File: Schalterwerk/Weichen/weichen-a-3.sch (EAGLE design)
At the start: 24 parts, among them Q1 P-MOSFET, Q2 P-MOSFET, X1 PHNX_4P_508CONN_1017493, X2 IO-HAT, X3 PHNX_4P_350CONN_1984989_PXC, X4 PHNX_4P_350CONN_1984989_PXC, X5 RJ45-JACK

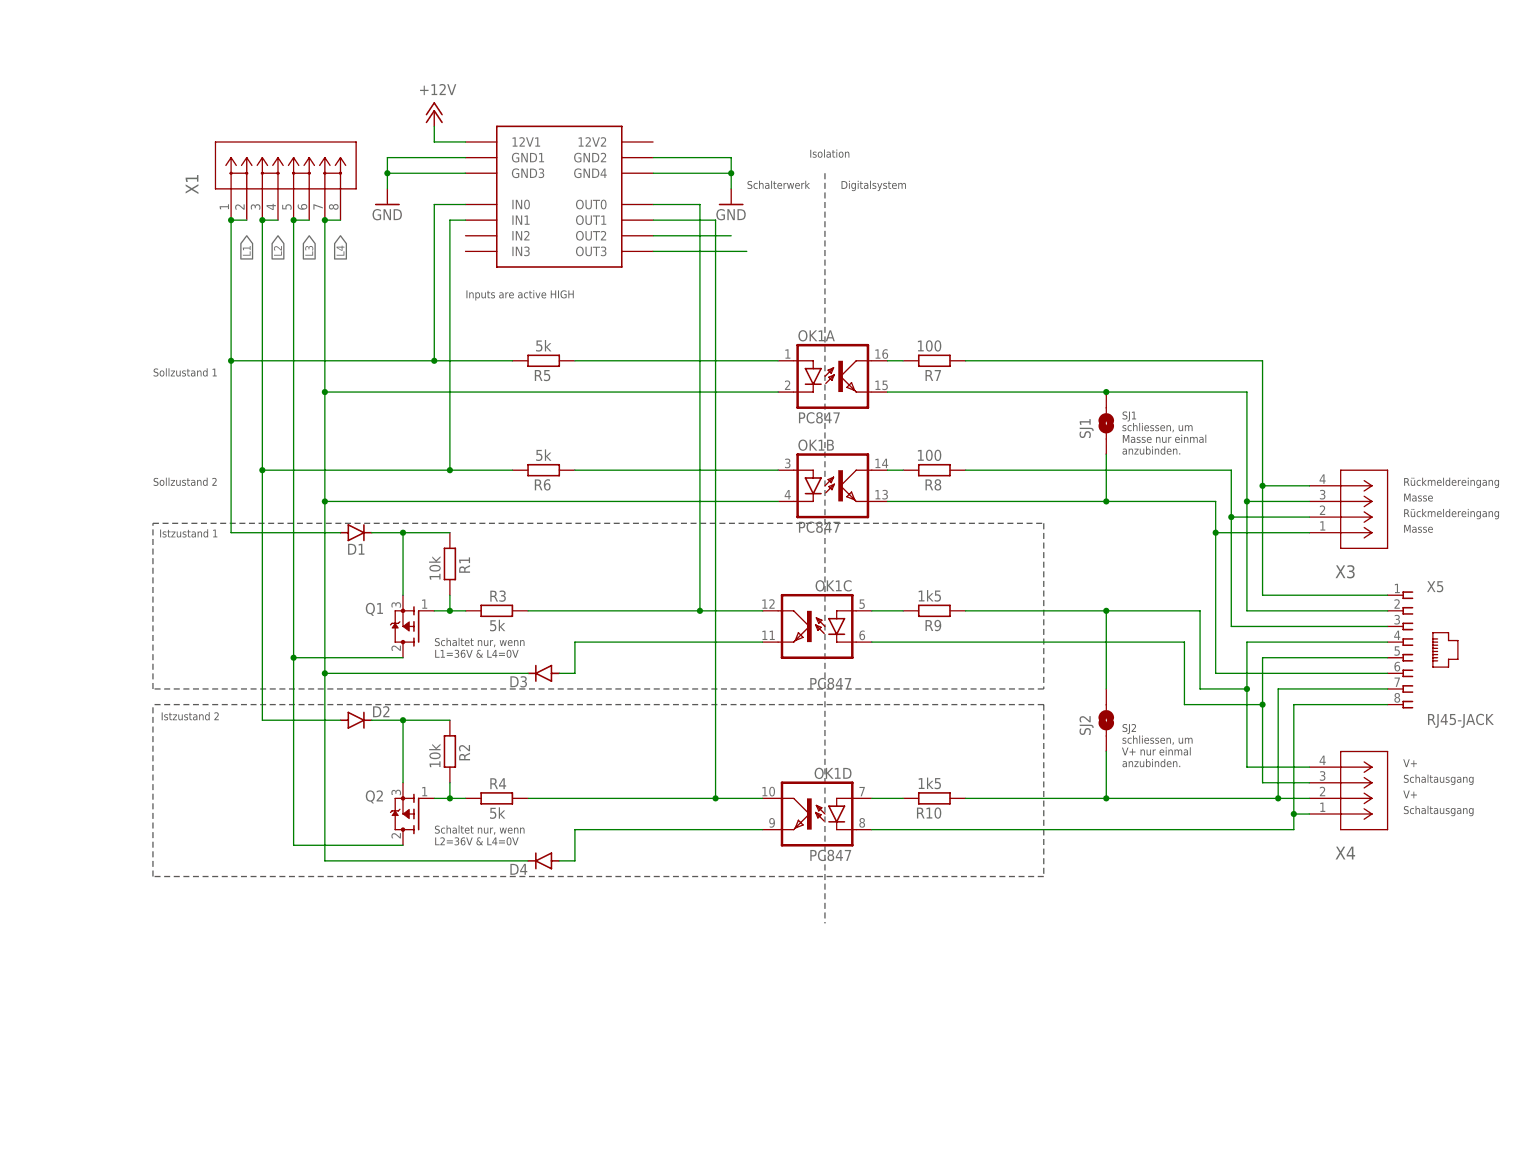
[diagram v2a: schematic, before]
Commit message: Adds all display LEDs, completes layout.
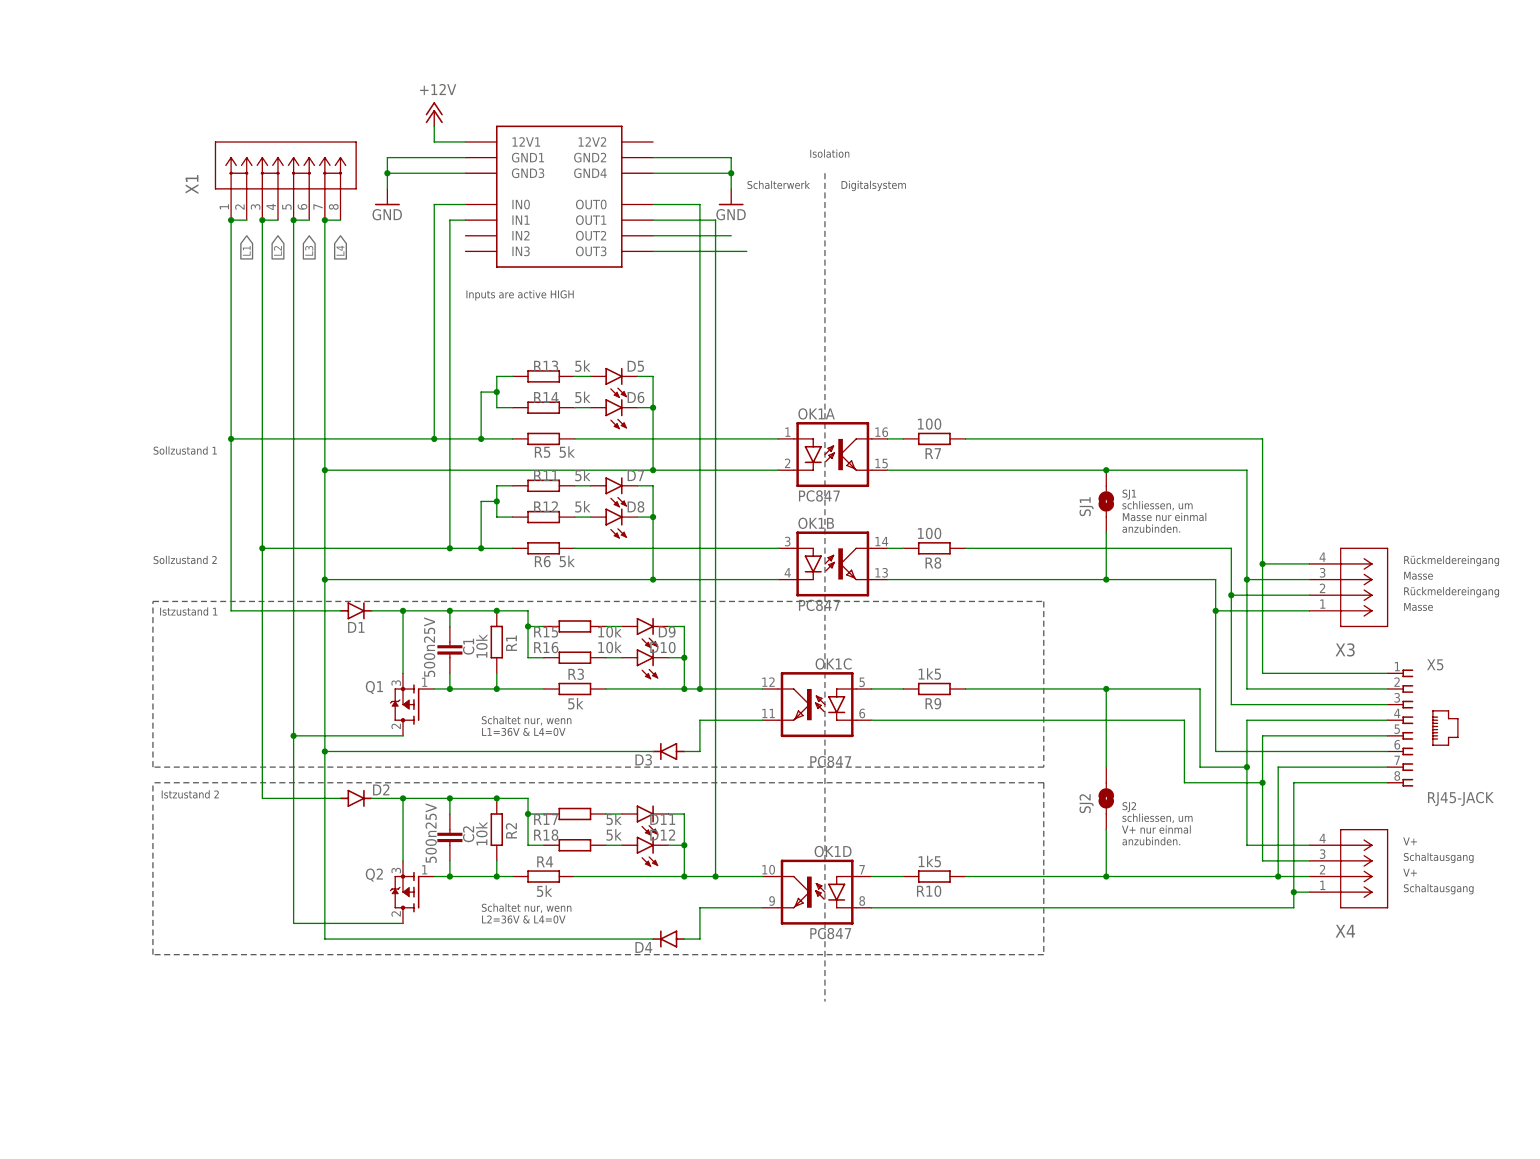
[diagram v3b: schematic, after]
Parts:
- added C1, C2: 500n25V, rcl:C-EUC0805
- added D10, D12, D6, D8: LEDHEADER, eagleparts:LEDHEADER
- added D11, D5, D7, D9: (no value), led:LEDCHIPLED_0603
- added R11, R12, R13, R14, R17, R18: 5k, rcl:R-EU_R0805
- added R15, R16: 10k, rcl:R-EU_R0805
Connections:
- removed net N$15: OK1C.COL, R3.2, X2G$1.OUT0
- removed net N$16: OK1D.COL, R4.2, X2G$1.OUT1
- removed net N$9: Q1.G, R1.2, R3.1
- new net IST1: D10.C, D9.C, OK1C.COL, R3.2, X2G$1.OUT0
- new net IST2: D11.C, D12.C, OK1D.COL, R4.2, X2G$1.OUT1
- new net N$10: D8.A, R12.1
- new net N$11: D9.A, R15.1
- new net N$14: D10.A, R16.1
- new net N$18: D11.A, R17.1
- new net N$20: D12.A, R18.1
- new net N$23: C1.2, Q1.G, R1.2, R3.1
- new net N$3: D7.A, R11.1
- new net N$4: D5.A, R13.1
- new net N$6: D6.A, R14.1
- net L1: now also R13.2, R14.2
- net L2: now also R11.2, R12.2
- net L4: now also D5.C, D6.C, D7.C, D8.C
- net N$1: now also C2.1, R17.2, R18.2
- net N$12: now also C2.2
- net N$13: now also C1.1, R15.2, R16.2
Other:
- moved on the sheet: D1, D2, D3, D4, OK1A, OK1B, OK1C, OK1D, Q1, Q2, R1, R10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

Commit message: Adds ports to connect adjacent boards. Adds ground pour.
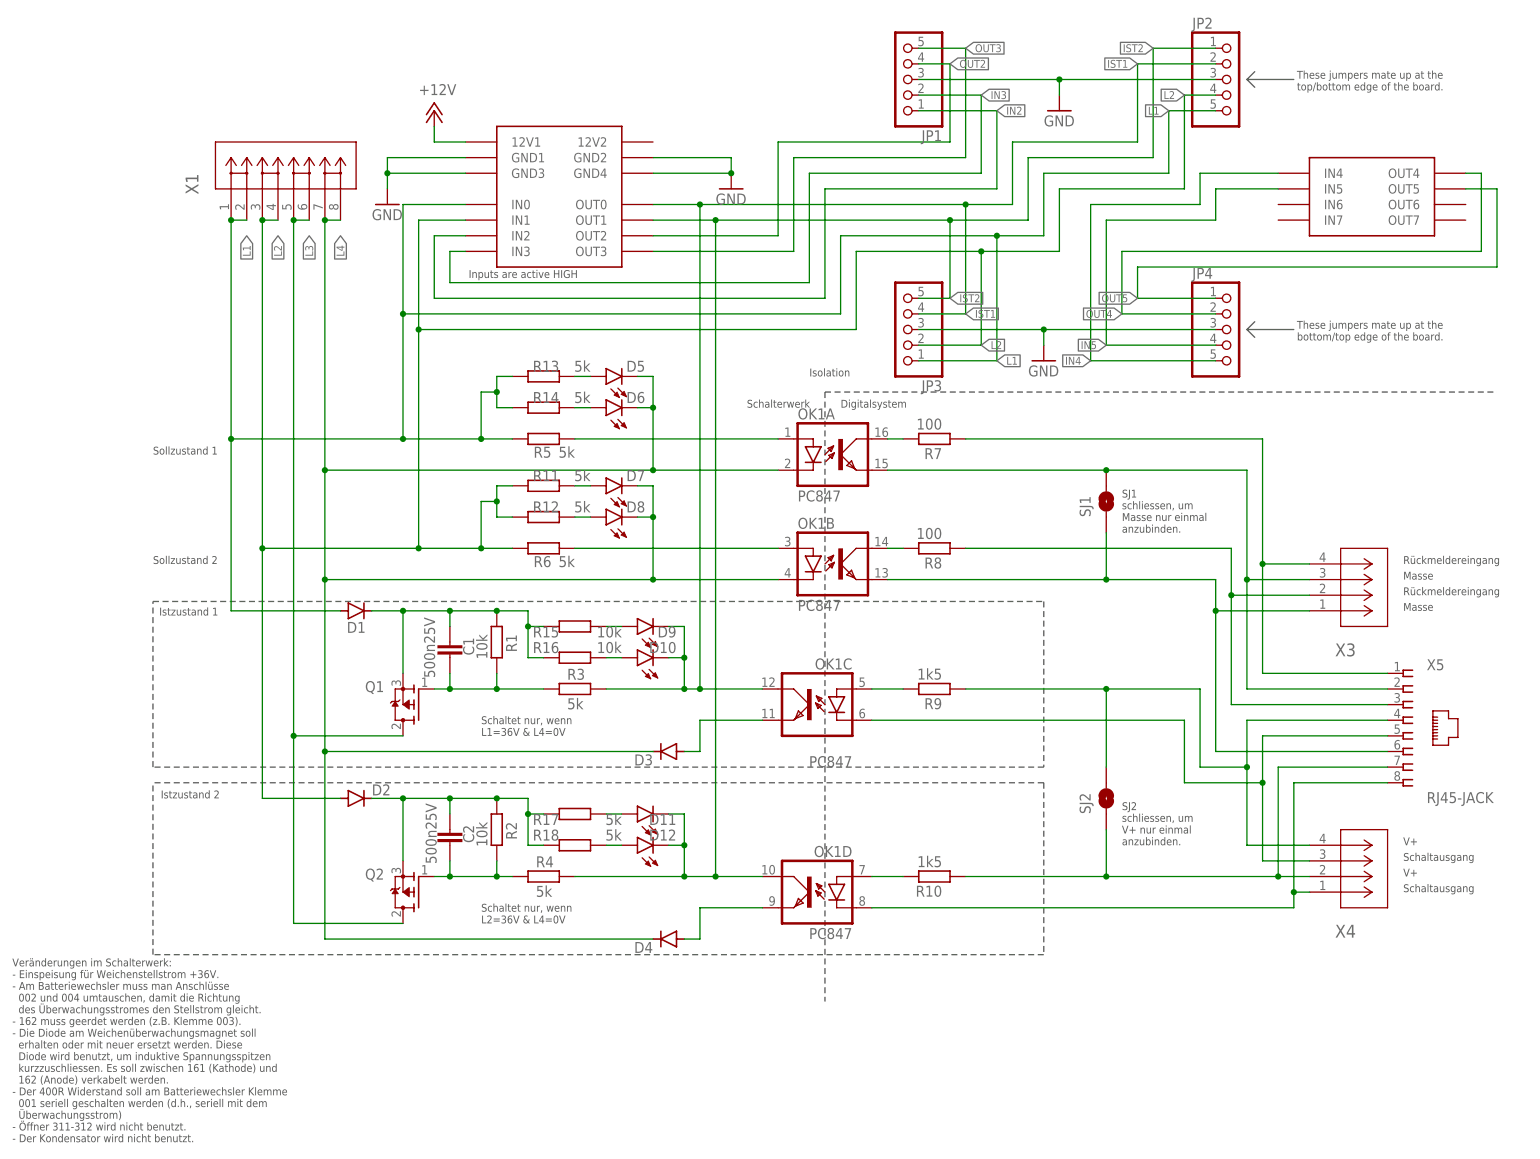
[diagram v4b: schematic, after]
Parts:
- added JP1, JP2, JP3, JP4: (no value), pinhead:PINHD-1X55X2MM
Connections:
- removed net N$24: X2G$1.OUT2
- removed net N$25: X2G$1.OUT3
- new net IN2: JP1.1, X2G$1.IN2
- new net IN3: JP1.2, X2G$1.IN3
- new net IN4: JP4.5, X2G$2.IN4
- new net IN5: JP4.4, X2G$2.IN5
- new net OUT2: JP1.4, X2G$1.OUT2
- new net OUT3: JP1.5, X2G$1.OUT3
- new net OUT4: JP4.2, X2G$2.OUT4
- new net OUT5: JP4.1, X2G$2.OUT5
- net GND: now also JP1.3, JP2.3, JP3.3, JP4.3
- net IST1: now also JP2.2, JP3.4
- net IST2: now also JP2.1, JP3.5
- net L1: now also JP2.5, JP3.1
- net L2: now also JP2.4, JP3.2
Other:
- note added: "These jumpers mate up at the bottom/top edge of the board."
- note added: "These jumpers mate up at the top/bottom edge of the board."
- note added: "Veränderungen im Schalterwerk: - Einspeisung für Weichenstellstrom +36V. - Am Batteriewechsler muss man Anschlüsse 002 und 004 umtauschen, damit die Richtung des Überwachungsstromes den Stellstrom gleicht. - 162 muss geerdet werden (z.B. Klemme 003). - Die Diode am Weichenüberwachungsmagnet soll erhalten oder mit neuer ersetzt werden. Diese Diode wird benutzt, um induktive Spannungsspitzen kurzzu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"
